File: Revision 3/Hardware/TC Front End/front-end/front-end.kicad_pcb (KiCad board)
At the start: 6 copper layers, 65 x 35 mm, 18 parts, among them J1 Conn_01x02, J2 4DB-P108-02, J5 Conn_01x04, U1 LM321, U2 LM321, U3 DS18B20+

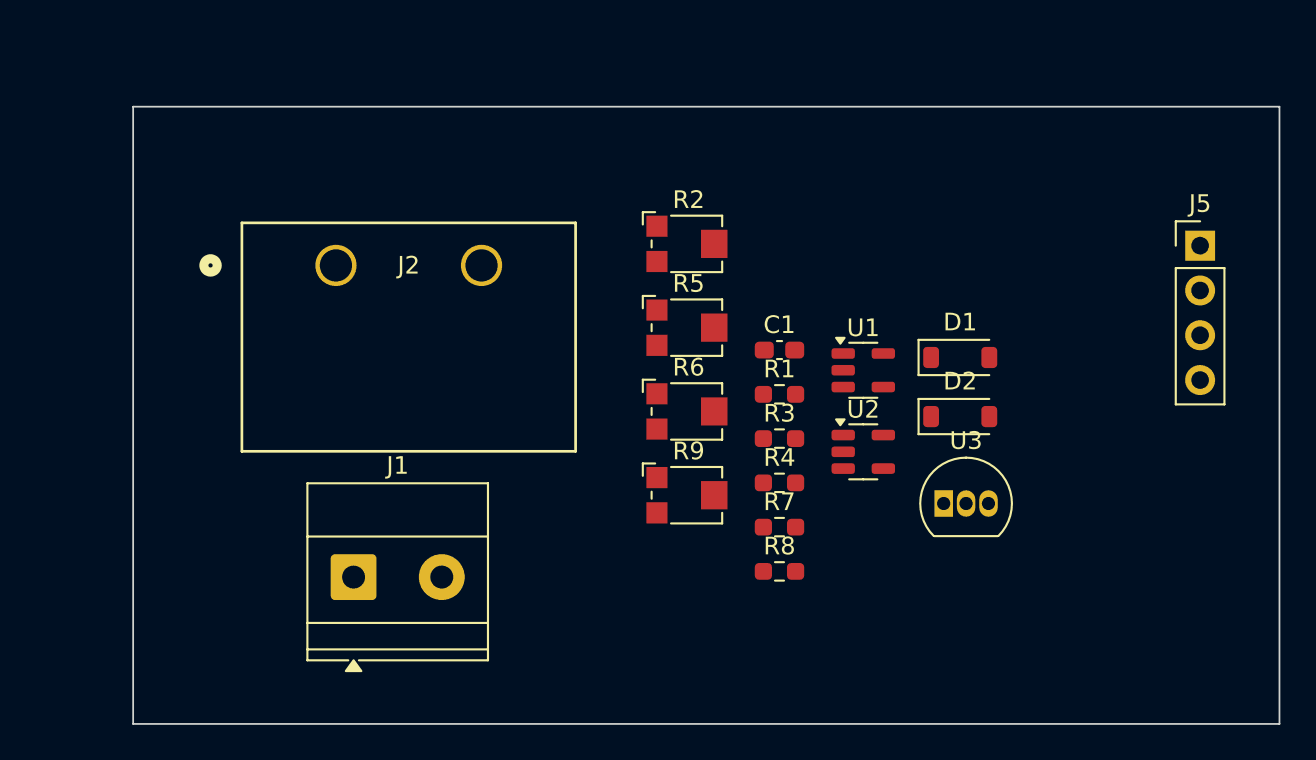
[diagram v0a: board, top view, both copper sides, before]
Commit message: PCB layout complete, ready for routing
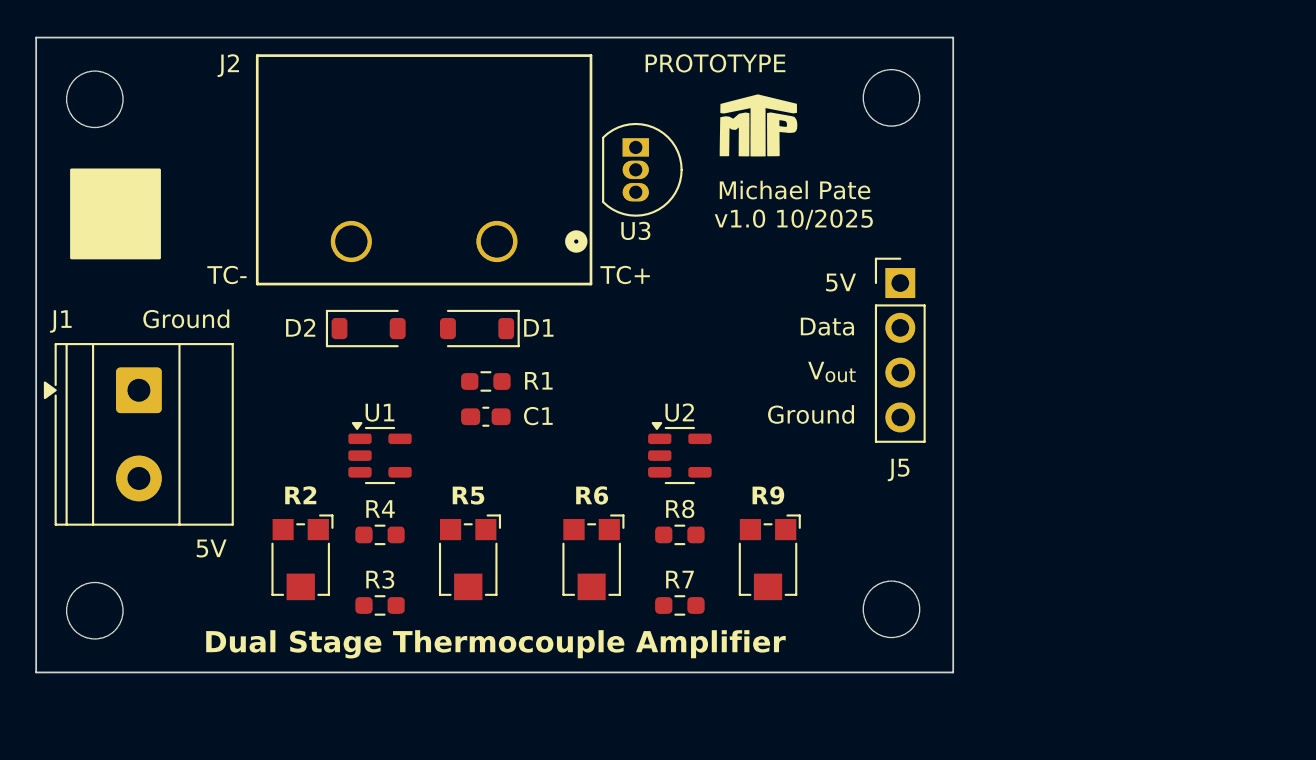
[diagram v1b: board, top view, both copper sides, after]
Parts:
- added H1: MountingHole, MountingHole:MountingHole_3.2mm_M3, F.Cu at (116.8, 92.6)
- added H2: MountingHole, MountingHole:MountingHole_3.2mm_M3, F.Cu at (162.0, 92.5)
- added H3: MountingHole, MountingHole:MountingHole_3.2mm_M3, F.Cu at (162.0, 121.5)
- added H4: MountingHole, MountingHole:MountingHole_3.2mm_M3, F.Cu at (116.8, 121.6)
- added REF**: MTP Logo 5mm Low Detail, Watermarks:MTP Logo 5mm Low Detail, F.Cu at (154.5, 94.6)
- moved D2 33.9 mm to (132.3, 105.6)
- moved R2 28.4 mm to (128.5, 118.8), turned to -90 degrees
- moved U1 27.8 mm to (133.0, 112.8)
- moved D1 27.4 mm to (138.5, 105.6), turned to 180 degrees
- moved U3 26.7 mm to (147.5, 95.3), turned to -90 degrees
- moved R3 24.5 mm to (133.0, 121.3)
- moved R4 22.8 mm to (133.0, 117.3)
- moved R5 18.2 mm to (138.0, 118.8), turned to -90 degrees
- moved J5 17.1 mm to (162.5, 103.0)
- moved C1 17.1 mm to (139.0, 110.6)
- moved R1 16.7 mm to (139.0, 108.6), turned to 180 degrees
- moved J1 16.1 mm to (119.3, 109.1), turned to -90 degrees
- moved U2 10.4 mm to (150.0, 112.8)
- moved R6 10.1 mm to (145.0, 118.8), turned to -90 degrees
- moved J2 9.23 mm to (139.6, 100.6), turned to 180 degrees
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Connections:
- J2 pad 1: GND -> Net-(D1-K)
- J2 pad 2: Net-(D1-K) -> GND
- R5 pad 1: Net-(R4-Pad2) -> Net-(U2-+)
- R5 pad 2: Net-(U2-+) -> Net-(R4-Pad2)
- R9 pad 1: Net-(R8-Pad2) -> Net-(J5-Pin_3)
- R9 pad 2: Net-(J5-Pin_3) -> Net-(R8-Pad2)
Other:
- board size 65 x 35 mm -> 52 x 36 mm
- board text added: "5V"
- board text added: "Data"
- board text added: "Dual Stage Thermocouple Amplifier"
- board text added: "Ground"
- board text added: "Michael Pate v1.0 10/2025"
- board text added: "PROTOTYPE"
- board text added: "TC+"
- board text added: "TC-"
- board text added: "V_{out}"

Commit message: PCB routing complete, ready for production
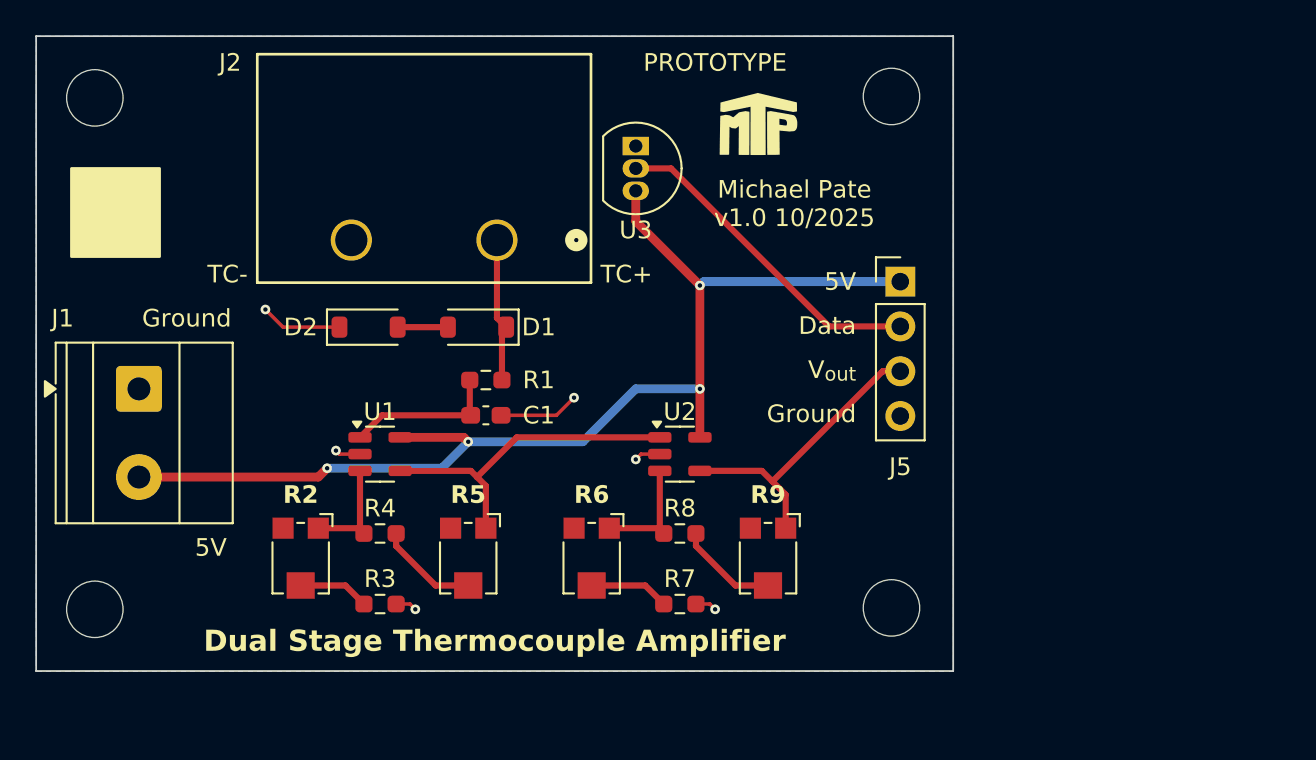
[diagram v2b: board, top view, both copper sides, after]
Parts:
- moved J2 0.08 mm to (139.6, 100.6)
- moved C1 0.08 mm to (139.0, 110.5)
- moved D1 0.08 mm to (138.5, 105.5)
- moved D2 0.08 mm to (132.3, 105.5)
- moved H1 0.08 mm to (116.8, 92.5)
- moved H2 0.08 mm to (162.0, 92.4)
- moved H3 0.08 mm to (162.0, 121.4)
- moved H4 0.08 mm to (116.8, 121.5)
- moved J1 0.08 mm to (119.3, 109.0)
- moved J5 0.08 mm to (162.5, 102.9)
- moved R1 0.08 mm to (139.0, 108.5)
- moved R2 0.08 mm to (128.5, 118.7)
- moved R3 0.08 mm to (133.0, 121.2)
- moved R4 0.08 mm to (133.0, 117.2)
- moved R5 0.08 mm to (138.0, 118.7)
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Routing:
- net +5V: track 0.00 -> 64.8 mm, vias 0 -> 4
- net Net-(U2-+): track 0.00 -> 18.9 mm
- net Net-(J5-Pin_2): track 0.00 -> 18.7 mm
- net Net-(J5-Pin_3): track 0.00 -> 17.2 mm
- net GND: track 0.00 -> 14.5 mm, vias 0 -> 6
- net Net-(U1-+): track 0.00 -> 8.81 mm
- net Net-(D1-K): track 0.00 -> 8.25 mm
- net Net-(U2--): track 0.00 -> 6.85 mm
- net Net-(U1--): track 0.00 -> 6.35 mm
- net Net-(R8-Pad2): track 0.00 -> 5.73 mm
- net Net-(R4-Pad2): track 0.00 -> 5.73 mm
- net Net-(R6-Pad2): track 0.00 -> 4.52 mm
- net Net-(R2-Pad2): track 0.00 -> 4.02 mm
- net Net-(D1-A): track 0.00 -> 2.85 mm
- added copper zone on B.Cu, net GND
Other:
- copper layers 6 -> 2

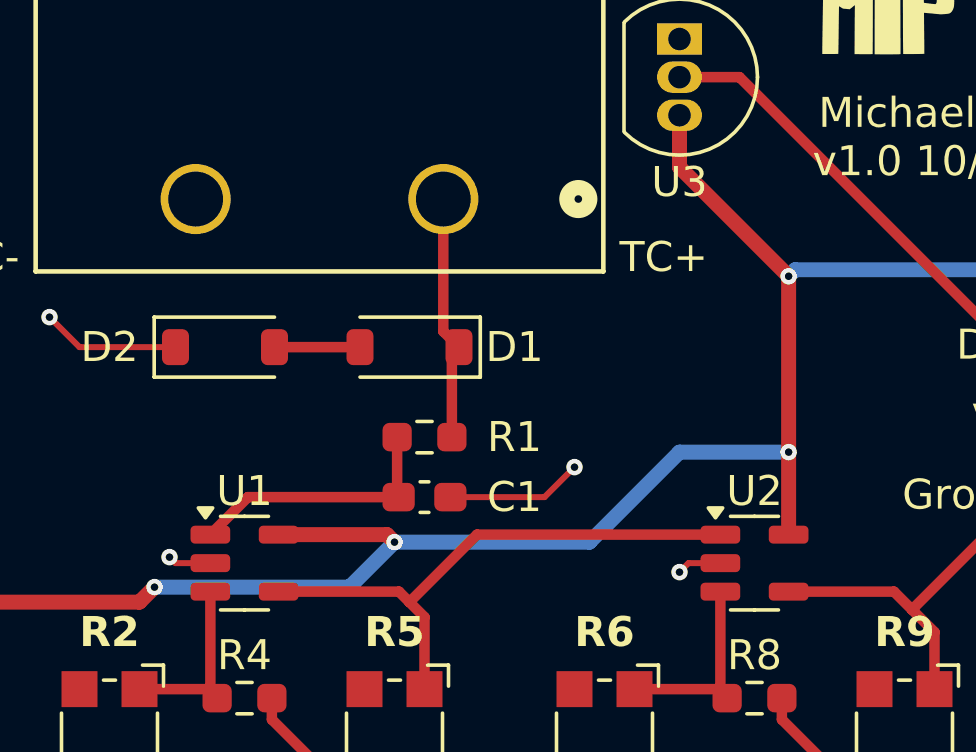
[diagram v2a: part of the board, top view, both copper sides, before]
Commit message: Add test points for inter stages
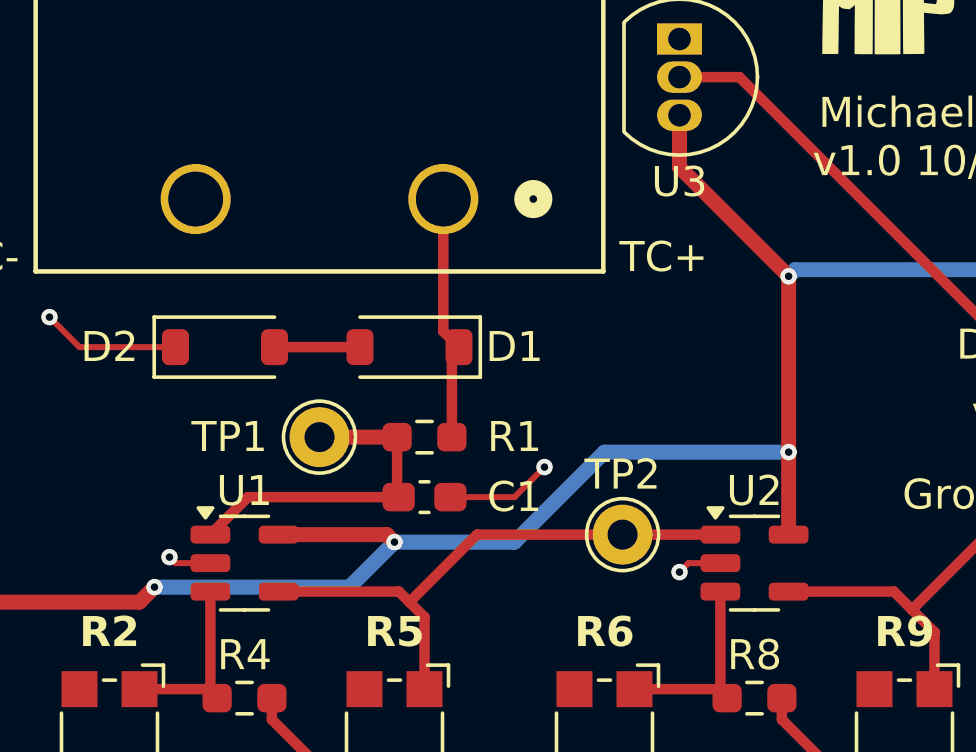
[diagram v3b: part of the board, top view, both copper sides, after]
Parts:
- added TP1: TestPoint, TestPoint:TestPoint_THTPad_D2.0mm_Drill1.0mm, F.Cu at (135.5, 108.5)
- added TP2: TestPoint, TestPoint:TestPoint_THTPad_D2.0mm_Drill1.0mm, F.Cu at (145.6, 111.8)
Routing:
- net Net-(U1-+): track 8.81 -> 11.4 mm
- net GND: track 14.5 -> 13.5 mm

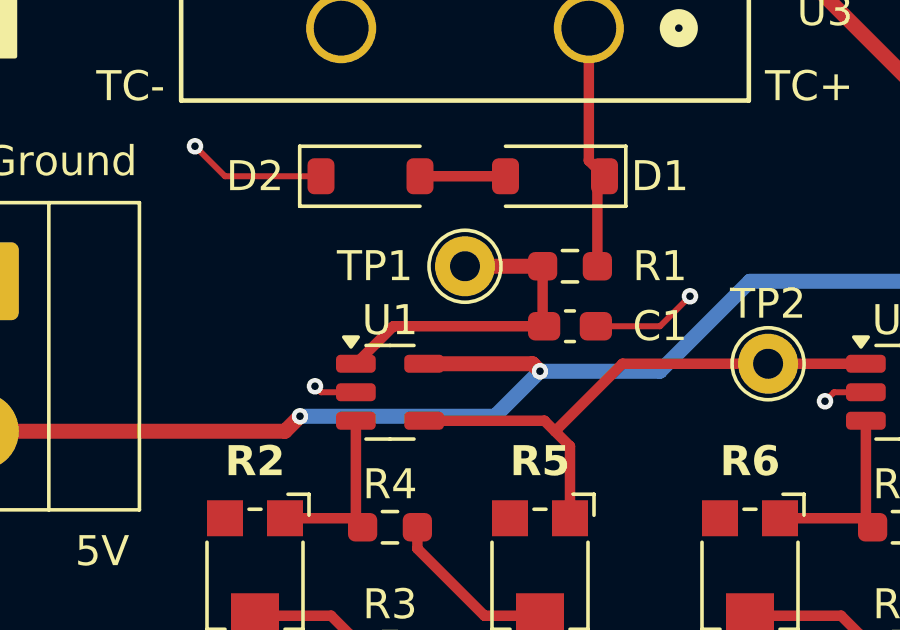
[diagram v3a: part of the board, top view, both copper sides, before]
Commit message: Sent PCB to production, add images to schematic
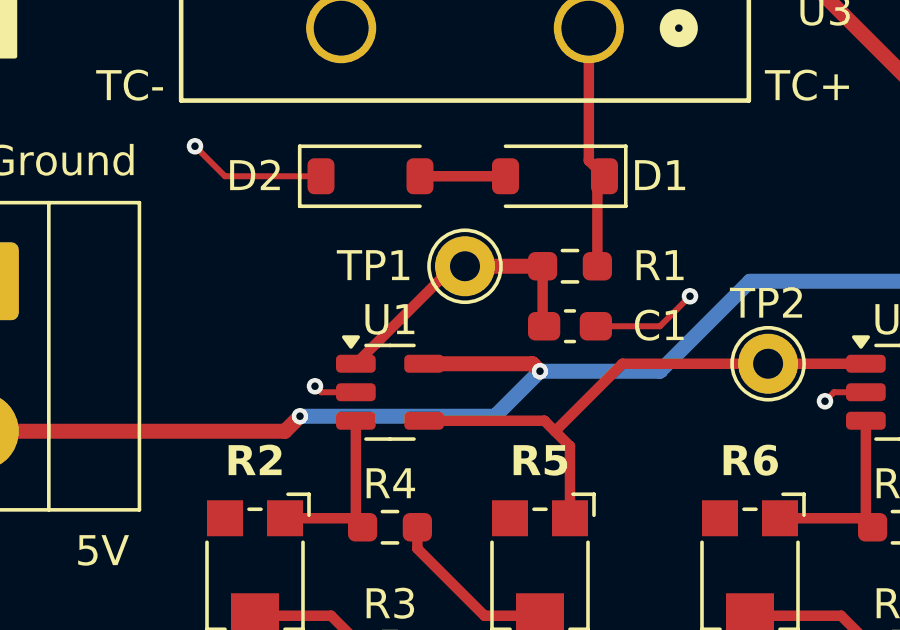
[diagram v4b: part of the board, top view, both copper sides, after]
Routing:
- net Net-(U1-+): track 11.4 -> 10.2 mm
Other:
- board text added: "TP1"
- board text added: "TP2"
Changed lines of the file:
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@@
+		)
+	)
+	(gr_text "TP1"
+		(at 132.5 108.5 -0)
+		(layer "B.SilkS")
+		(effects
+			(font
+				(size 1 1)
+				(thickness 0.15)
+			)
+			(justify mirror)
 		)
 	)
@@
 	(gr_text "TC-"
 		(at 131.5 97.5 0)
+		(layer "B.SilkS")
+		(effects
+			(font
+				(size 1 1)
+				(thickness 0.15)
+			)
+			(justify mirror)
+		)
+	)
+	(gr_text "TP2"
+		(at 145.587312 109.748242 -0)
 		(layer "B.SilkS")
 		(effects
@@
 	)
 	(segment
-		(start 133.1125 110.5)
+		(start 136.1375 108.5)
+		(end 135.1125 108.5)
+		(width 0.35)
+		(layer "F.Cu")
+		(net 1)
+	)
+	(segment
+		(start 135.1125 108.5)
 		(end 131.8625 111.75)
 		(width 0.35)
@@
 		(layer "F.Cu")
 		(net 1)
-	)
-	(segment
-		(start 138.1375 110.5)
-		(end 133.1125 110.5)
-		(width 0.35)
-		(layer "F.Cu")
-		(net 1)
